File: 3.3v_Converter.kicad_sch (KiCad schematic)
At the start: 0 parts

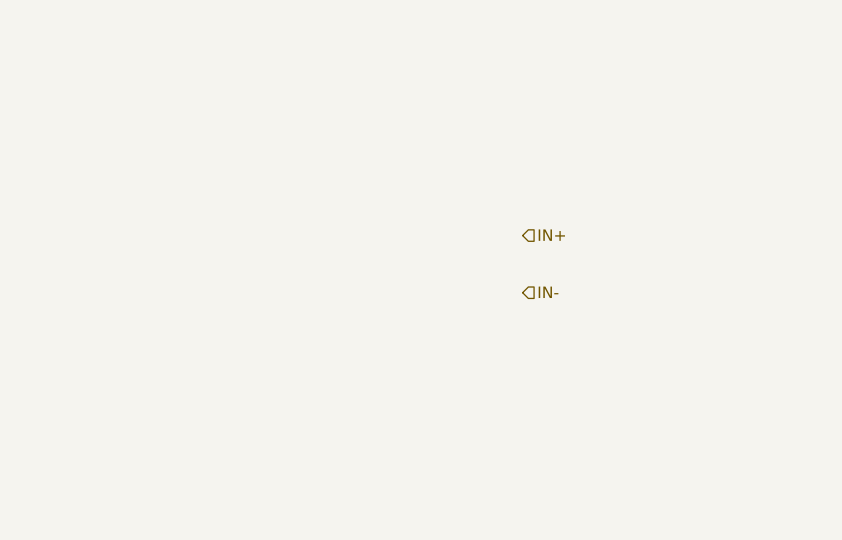
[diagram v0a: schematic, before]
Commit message: "3.3V buck boost converter added. few footprints added"
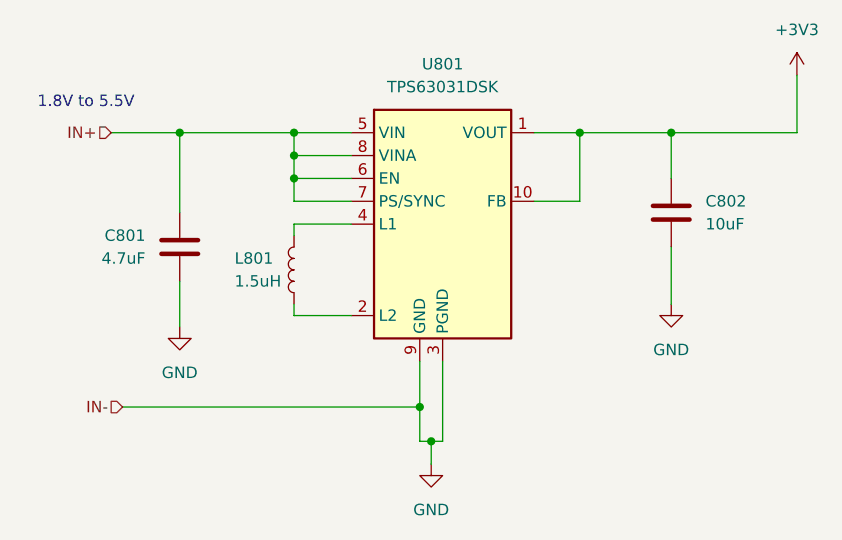
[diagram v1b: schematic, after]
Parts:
- added C801: 4.7uF, symbol Device:C
- added C802: 10uF, symbol Device:C
- added L801: 1.5uH, symbol Device:L
- added U801: TPS63031DSK, Package_SON:WSON-10-1EP_2.5x2.5mm_P0.5mm_EP1.2x2mm, symbol Regulator_Switching:TPS63031DSK
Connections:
- net IN+: now also C801.1, U801.5 (VIN), U801.6 (EN), U801.7 (PS/SYNC), U801.8 (VINA)
- new net: L801.2, U801.2 (L2)
- new net: L801.1, U801.4 (L1)
- new net +3V3: C802.1, U801.1 (VOUT), U801.10 (FB)
- new net GND: C801.2, C802.2, U801.11 (PGND), U801.3 (PGND), U801.9 (GND)
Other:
- note added: "1.8V to 5.5V"
